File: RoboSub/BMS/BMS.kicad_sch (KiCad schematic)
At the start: 30 parts, among them J1 battery, J2 temp, J3 ExtPwrSw, J4 output, J5 CAN, K1 A31CSP12VDC2D, Q1 PMV28ENEA, SW1 DBG2, SW2 DBG1, SW3 RST, U2 CZ3A07, U5 PCC

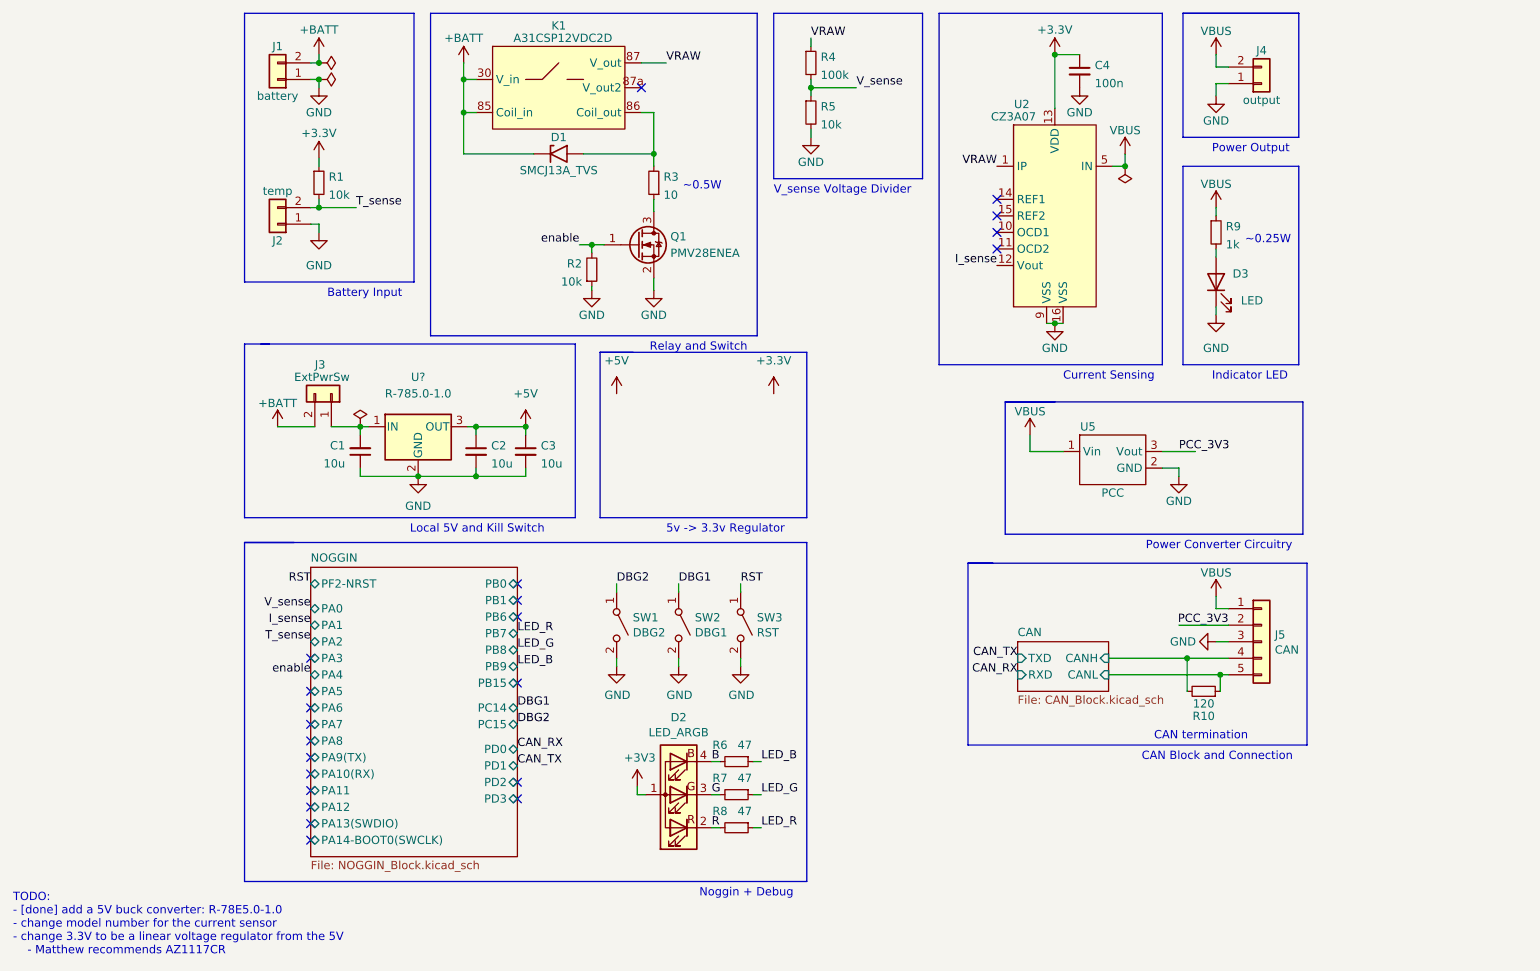
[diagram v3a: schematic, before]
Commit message: added 5V real for current sense. Also added 5v->3.3v LDO.
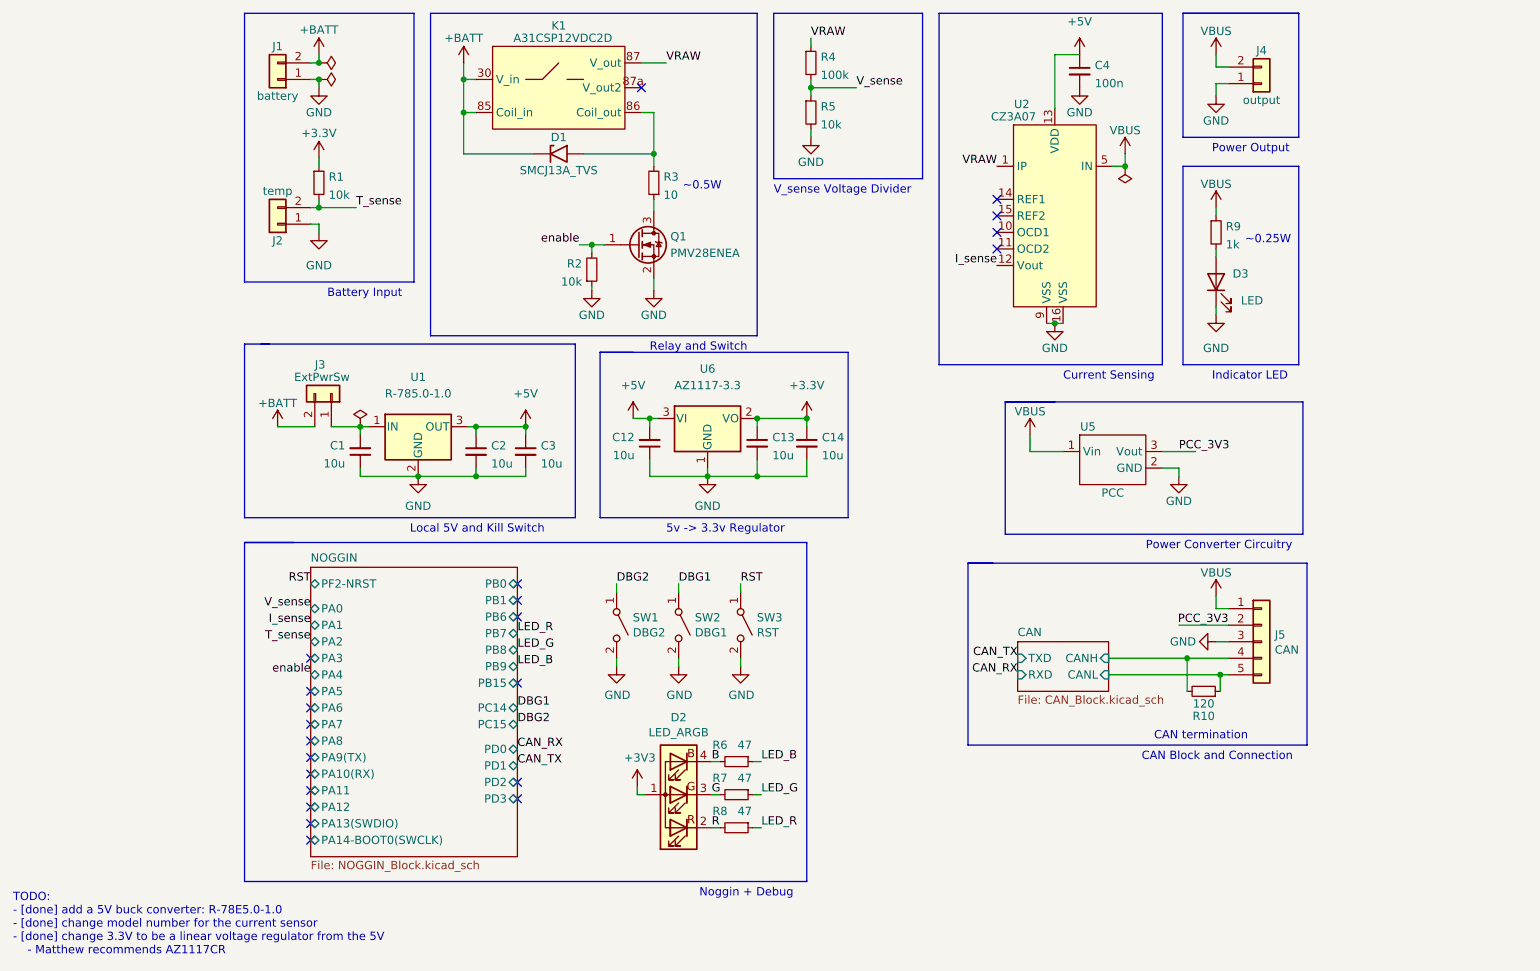
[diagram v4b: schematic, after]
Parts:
- added C12, C13, C14: 10u, Capacitor_SMD:C_0805_2012Metric, symbol Device:C_Small
- added U6: AZ1117-3.3, symbol Regulator_Linear:AZ1117-3.3
- gave numbers to parts that had none: 1
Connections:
- net +3V3: now also C13.1, C14.1, U6.2 (VO); no longer C4.1, U2.13 (VDD)
- net +5V: now also C4.1, U2.13 (VDD), C12.2, U6.3 (VI)
- net GND: now also C12.1, C13.2, C14.2, U6.1 (GND)
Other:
- note added: "TODO: - [done] add a 5V buck converter: R-78E5.0-1.0 - [done] change model number for the current sensor - [done] change 3.3V to be a linear voltage regulator from the 5V - Matthew recommends AZ1117CR"
- note removed: "TODO: - [done] add a 5V buck converter: R-78E5.0-1.0 - change model number for the current sensor - change 3.3V to be a linear voltage regulator from the 5V - Matthew recommends AZ1117CR"

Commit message: Finished Layout for the BMS
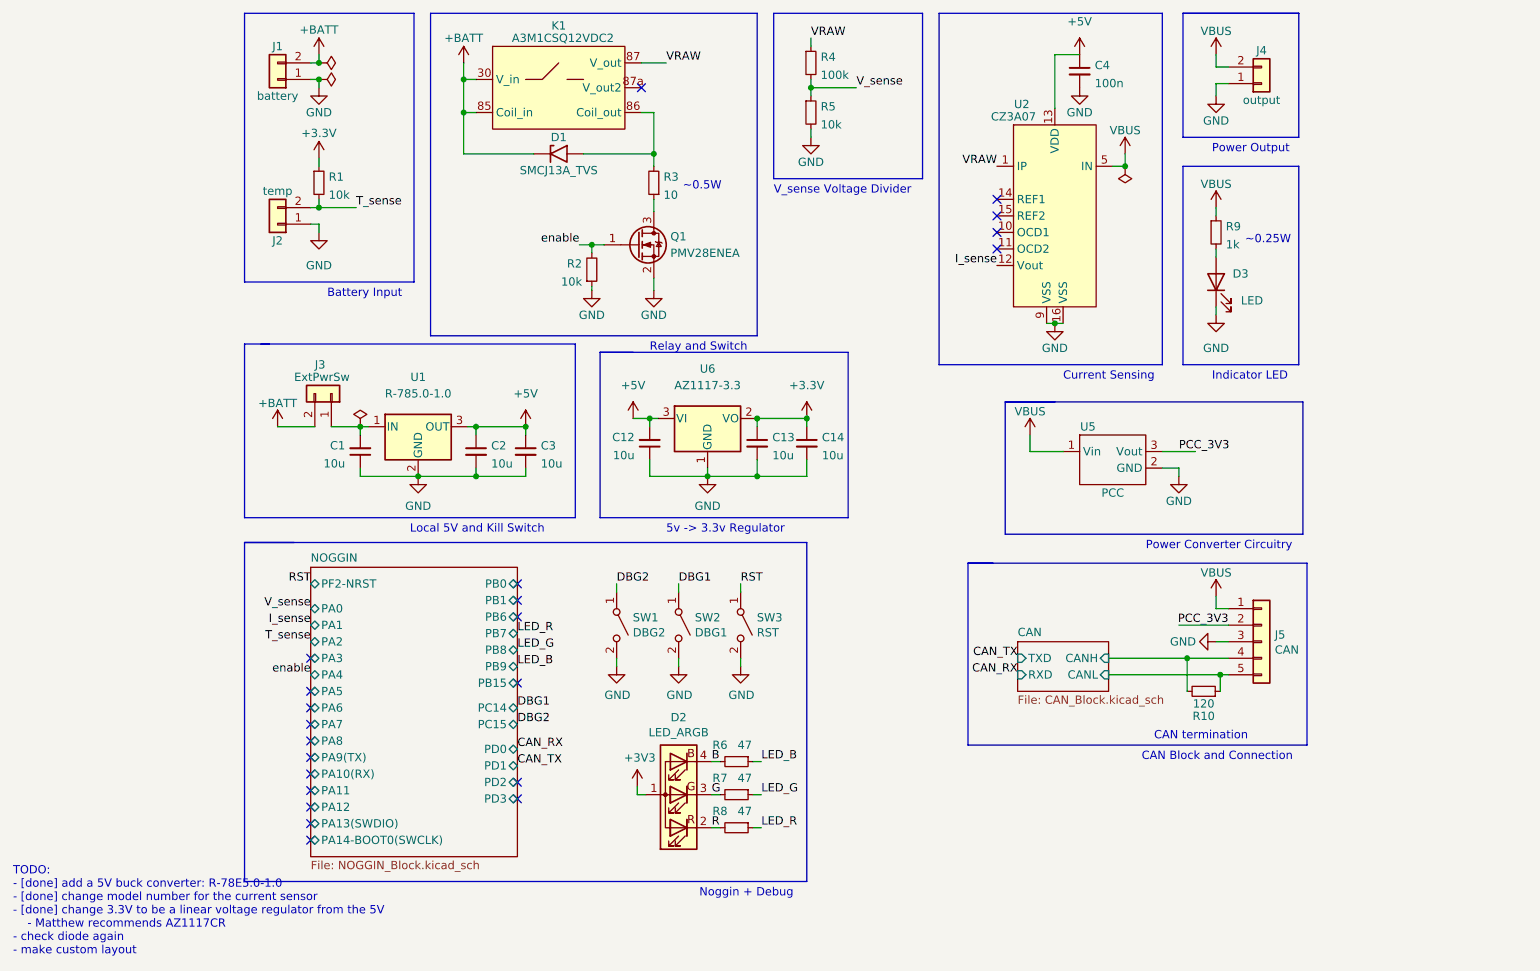
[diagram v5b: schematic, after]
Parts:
- K1: value A31CSP12VDC2D -> A3M1CSQ12VDC2; footprint BMS_Library:A3_Relay -> BMS_Library:A3M1CSQ12VDC2
- U6: footprint (none) -> Package_TO_SOT_SMD:SOT-89-3_Handsoldering
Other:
- note added: "TODO: - [done] add a 5V buck converter: R-78E5.0-1.0 - [done] change model number for the current sensor - [done] change 3.3V to be a linear voltage regulator from the 5V - Matthew recommends AZ1117CR - check diode again - make custom layout"
- note removed: "TODO: - [done] add a 5V buck converter: R-78E5.0-1.0 - [done] change model number for the current sensor - [done] change 3.3V to be a linear voltage regulator from the 5V - Matthew recommends AZ1117CR"
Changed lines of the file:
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@@
     (effects (font (size 1.27 1.27)) (justify left bottom))
   )
-  (text "TODO:\n- [done] add a 5V buck converter: R-78E5.0-1.0\n- [done] change model number for the current sensor\n- [done] change 3.3V to be a linear voltage regulator from the 5V\n	- Matthew recommends AZ1117CR\n"
+  (text "TODO:\n- [done] add a 5V buck converter: R-78E5.0-1.0\n- [done] change model number for the current sensor\n- [done] change 3.3V to be a linear voltage regulator from the 5V\n	- Matthew recommends AZ1117CR\n- check diode again\n- make custom layout\n"
     (at 29.21 171.45 0)
     (effects (font (size 1.27 1.27)) (justify left bottom))
@@
     (property "Reference" "U6" (id 0) (at 135.89 81.28 0))
     (property "Value" "AZ1117-3.3" (id 1) (at 135.89 83.82 0))
-    (property "Footprint" "" (id 2) (at 135.89 82.55 0)
+    (property "Footprint" "Package_TO_SOT_SMD:SOT-89-3_Handsoldering" (id 2) (at 135.89 82.55 0)
       (effects (font (size 1.27 1.27) italic) hide)
     )
@@
     (in_bom yes) (on_board yes)
     (property "Reference" "K1" (id 0) (at 113.03 28.575 0))
-    (property "Value" "A31CSP12VDC2D" (id 1) (at 113.665 30.48 0))
-    (property "Footprint" "BMS_Library:A3_Relay" (id 2) (at 113.03 35.56 0)
+    (property "Value" "A3M1CSQ12VDC2" (id 1) (at 113.665 30.48 0))
+    (property "Footprint" "BMS_Library:A3M1CSQ12VDC2" (id 2) (at 113.03 35.56 0)
       (effects (font (size 1.27 1.27)) hide)
     )
@@
     )
     (path "/25ee2213-f0fe-4c7d-ac11-be4f26ffce69"
-      (reference "K1") (unit 1) (value "A31CSP12VDC2D") (footprint "BMS_Library:A3_Relay")
+      (reference "K1") (unit 1) (value "A3M1CSQ12VDC2") (footprint "BMS_Library:A3M1CSQ12VDC2")
     )
     (path "/96040761-b0e5-47a9-8ba7-7d9622476861"
@@
     )
     (path "/04115f07-479b-42d9-90c5-1e7be33dc7a6"
-      (reference "U6") (unit 1) (value "AZ1117-3.3") (footprint "")
-    )
-  )
+      (reference "U6") (unit 1) (value "AZ1117-3.3") (footprint "Package_TO_SOT_SMD:SOT-89-3_Handsoldering")
+    )
+  )

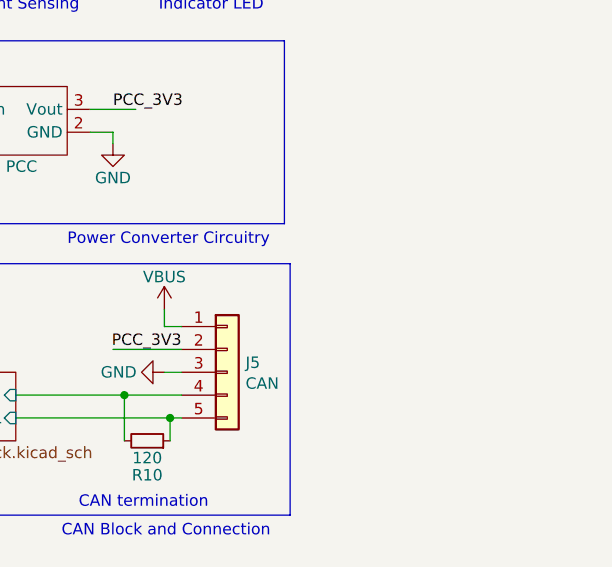
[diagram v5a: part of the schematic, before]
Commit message: created zones for the BAT, VRAW, VBUS and moved STM32 to back of board
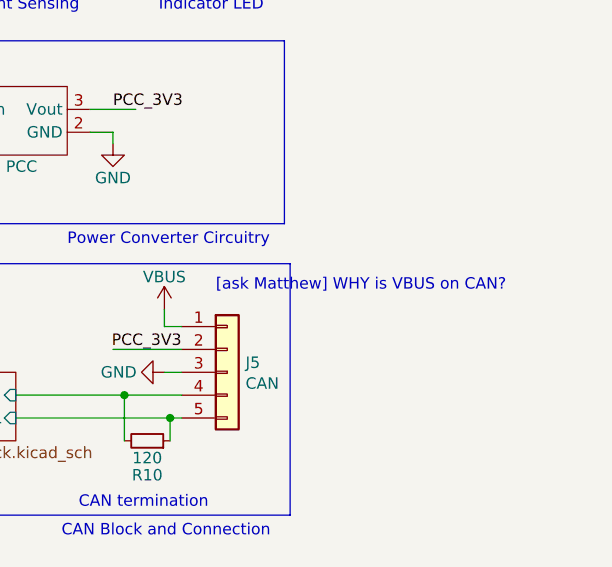
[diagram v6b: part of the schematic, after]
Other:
- note added: "[ask Matthew] WHY is VBUS on CAN?"
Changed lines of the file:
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@@
+    (effects (font (size 1.27 1.27)) (justify left bottom))
+  )
+  (text "[ask Matthew] WHY is VBUS on CAN?" (at 219.71 114.3 0)
     (effects (font (size 1.27 1.27)) (justify left bottom))
   )
